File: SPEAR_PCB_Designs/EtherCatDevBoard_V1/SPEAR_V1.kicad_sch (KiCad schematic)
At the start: 32 parts, among them J2 USB_C_Receptacle_USB2.0_16P, J3 Conn_01x21_Pin, J5 Conn_01x21_Pin, J6 FTSH-107-01-F-DV-K-P-TR, SW1 SW_Push, SW2 SW_Push, U1 STM32F446RCTx, U2 USBLC6-2SC6, U3 AMS1117-3.3, Y1 16MHz

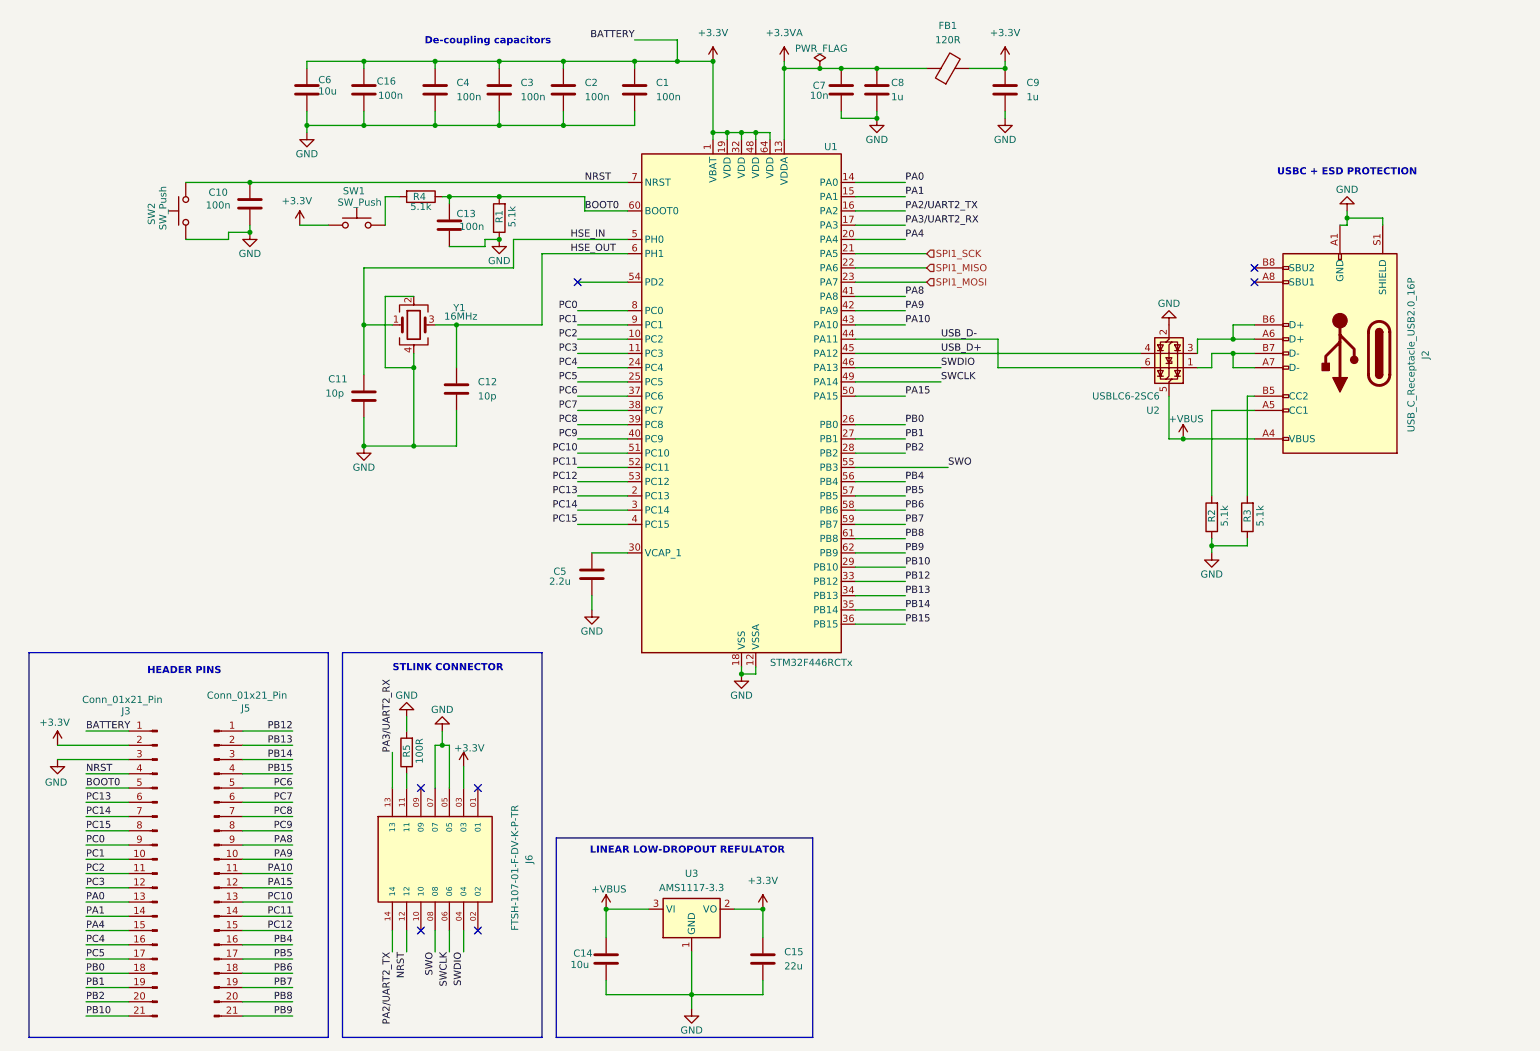
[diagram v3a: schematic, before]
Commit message: Update SPEAR_V1.kicad_sch
Footprints
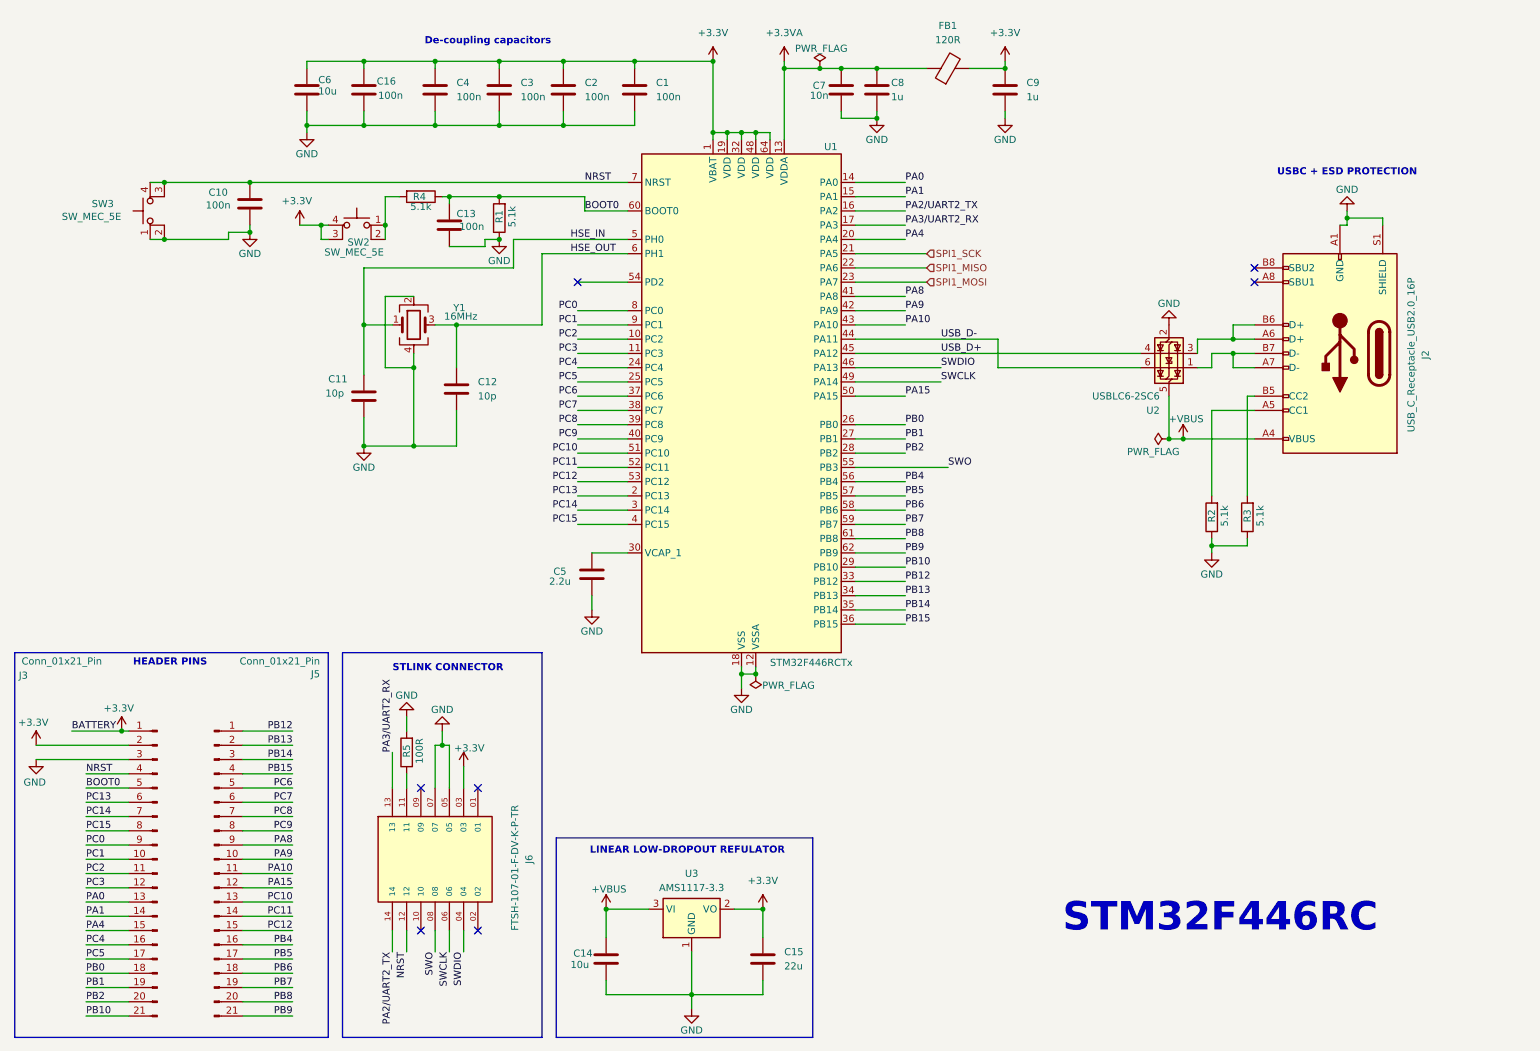
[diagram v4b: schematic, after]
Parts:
- removed SW1, SW2: SW_Push, symbol Switch:SW_Push
- added SW2, SW3: SW_MEC_5E, Button_Switch_SMD:SW_MEC_5GSH9, symbol Switch:SW_MEC_5E
- C1, C10, C11, C12, C13, C14, C16, C2, C3, C4, C5, C7, C8, C9: footprint (none) -> Capacitor_SMD:C_0402_1005Metric
- C15: footprint (none) -> Capacitor_SMD:C_0805_2012Metric
- C6: footprint (none) -> Capacitor_SMD:C_0603_1608Metric
- FB1: footprint (none) -> Inductor_SMD:L_0603_1608Metric
- J2: footprint (none) -> Connector_USB:USB_C_Receptacle_GCT_USB4105-xx-A_16P_TopMnt_Horizontal
- J3, J5: footprint (none) -> Connector_PinHeader_2.54mm:PinHeader_1x21_P2.54mm_Vertical
- J6: footprint FTSH-107-01-F-DV-K-P-TR:SAMTEC_FTSH-107-01-F-DV-K-P-TR -> Library:SAMTEC_FTSH-107-01-F-DV-K-P-TR
- R1, R2, R3, R4, R5: footprint (none) -> Resistor_SMD:R_0402_1005Metric
- Y1: footprint (none) -> Crystal:Crystal_SMD_2016-4Pin_2.0x1.6mm
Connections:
- net +3.3V: now also SW2.3 (K), SW2.4 (A)
- net GND: now also SW3.1, SW3.2
- net NRST: now also SW3.3 (K), SW3.4 (A)
- net at R4.2: now also SW2.1, SW2.2
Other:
- note added: "STM32F446RC"
- title: (none) -> SPEAR Development Board

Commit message: Updated Schematic and routing
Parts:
- removed C13: 100n, Capacitor_SMD:C_0402_1005Metric, symbol Device:C
- removed SW2, SW3: SW_MEC_5E, Button_Switch_SMD:SW_MEC_5GSH9, symbol Switch:SW_MEC_5E
- added D1: LED, LED_SMD:LED_0201_0603Metric, symbol Device:LED
- added R6: 5.1k, Resistor_SMD:R_0402_1005Metric, symbol Device:R
- added SW1: SW_Push, Button_Switch_SMD:SW_Tactile_SPST_NO_Straight_CK_PTS636Sx25SMTRLFS, symbol Switch:SW_Push
- R1: value 5.1k -> 10k
- R4: value 5.1k -> 100R
- Y1: footprint Crystal:Crystal_SMD_2016-4Pin_2.0x1.6mm -> Crystal:Crystal_SMD_3225-4Pin_3.2x2.5mm
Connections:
- net +3.3V: now also D1.2 (A)
- net BOOT0: now also R1.1; no longer J3.5 (Pin_5), R1.2, R4.1
- net GND: now also J3.4 (Pin_4), R1.2, R6.2, SW1.1; no longer R1.1
- net NRST: now also R4.1; no longer J3.4 (Pin_4)
- net PA0: now also J3.9 (Pin_9); no longer J3.13 (Pin_13)
- net PA1: now also J3.10 (Pin_10); no longer J3.14 (Pin_14)
- net PA10: now also J5.7 (Pin_7); no longer J5.11 (Pin_11)
- net PA15: now also J5.8 (Pin_8); no longer J5.12 (Pin_12)
- net PA4: now also J3.11 (Pin_11); no longer J3.15 (Pin_15)
- net PA8: now also J5.5 (Pin_5); no longer J5.9 (Pin_9)
- net PA9: now also J5.6 (Pin_6); no longer J5.10 (Pin_10)
- net PB0: now also J3.14 (Pin_14); no longer J3.18 (Pin_18)
- net PB1: now also J3.15 (Pin_15); no longer J3.19 (Pin_19)
- net PB10: now also J3.17 (Pin_17); no longer J3.21 (Pin_21)
- net PB12: now also J3.18 (Pin_18); no longer J5.1 (Pin_1)
- net PB13: now also J3.19 (Pin_19); no longer J5.2 (Pin_2)
- net PB14: now also J3.20 (Pin_20); no longer J5.3 (Pin_3)
- net PB15: now also J3.21 (Pin_21); no longer J5.4 (Pin_4)
- net PB2: now also J3.16 (Pin_16); no longer J3.20 (Pin_20)
- net PB4: now also J5.13 (Pin_13); no longer J5.16 (Pin_16)
- net PB5: now also J5.14 (Pin_14); no longer J5.17 (Pin_17)
- net PB6: now also J5.15 (Pin_15); no longer J5.18 (Pin_18)
- net PB7: now also J5.16 (Pin_16); no longer J5.19 (Pin_19)
- net PB8: now also J5.17 (Pin_17); no longer J5.20 (Pin_20)
- net PB9: now also J5.18 (Pin_18); no longer J5.21 (Pin_21)
- net PC0: now also J3.5 (Pin_5); no longer J3.9 (Pin_9)
- net PC1: now also J3.6 (Pin_6); no longer J3.10 (Pin_10)
- net PC10: now also J5.9 (Pin_9); no longer J5.13 (Pin_13)
- net PC11: now also J5.10 (Pin_10); no longer J5.14 (Pin_14)
- net PC12: now also J5.11 (Pin_11); no longer J5.15 (Pin_15)
- net PC13: now also J5.19 (Pin_19); no longer J3.6 (Pin_6)
- net PC14: now also J5.20 (Pin_20); no longer J3.7 (Pin_7)
- net PC15: now also J5.21 (Pin_21); no longer J3.8 (Pin_8)
- net PC2: now also J3.7 (Pin_7); no longer J3.11 (Pin_11)
- net PC3: now also J3.8 (Pin_8); no longer J3.12 (Pin_12)
- net PC4: now also J3.12 (Pin_12); no longer J3.16 (Pin_16)
- net PC5: now also J3.13 (Pin_13); no longer J3.17 (Pin_17)
- net PC6: now also J5.1 (Pin_1); no longer J5.5 (Pin_5)
- net PC7: now also J5.2 (Pin_2); no longer J5.6 (Pin_6)
- net PC8: now also J5.3 (Pin_3); no longer J5.7 (Pin_7)
- net PC9: now also J5.4 (Pin_4); no longer J5.8 (Pin_8)
- net at R4.2: now also SW1.2
- net PD2: now reaches U1.54 (PD2)
- net PD2: now also J5.12 (Pin_12)
- net USBC_D-: now reaches J2.A7 (D-), J2.B7 (D-), U2.1 (I/O1)
- net USBC_D+: now reaches J2.A6 (D+), J2.B6 (D+), U2.3 (I/O2)
- net +VBUS renamed +5V
- net PA2/UART2_TX renamed UART2_TX
- net PA3/UART2_RX renamed UART2_RX
- new net PWR_LED_K: D1.1 (K), R6.1
- no-connect marks 7 -> 6
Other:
- moved on the sheet: C10

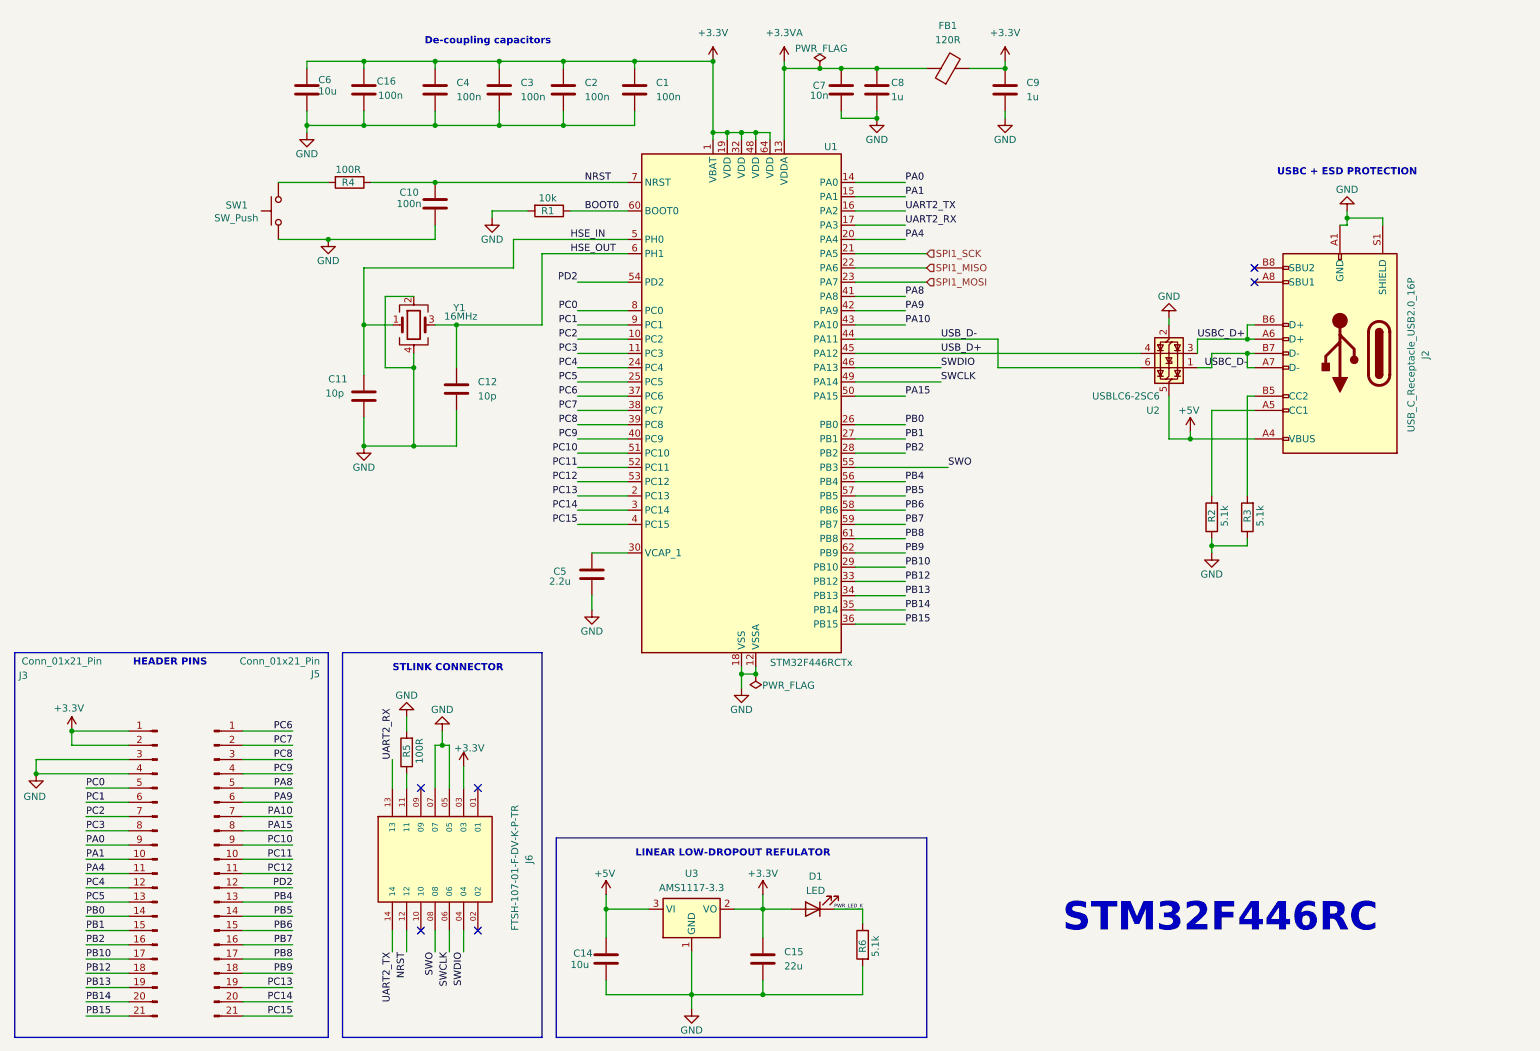
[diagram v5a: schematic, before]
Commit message: changes to lan setting
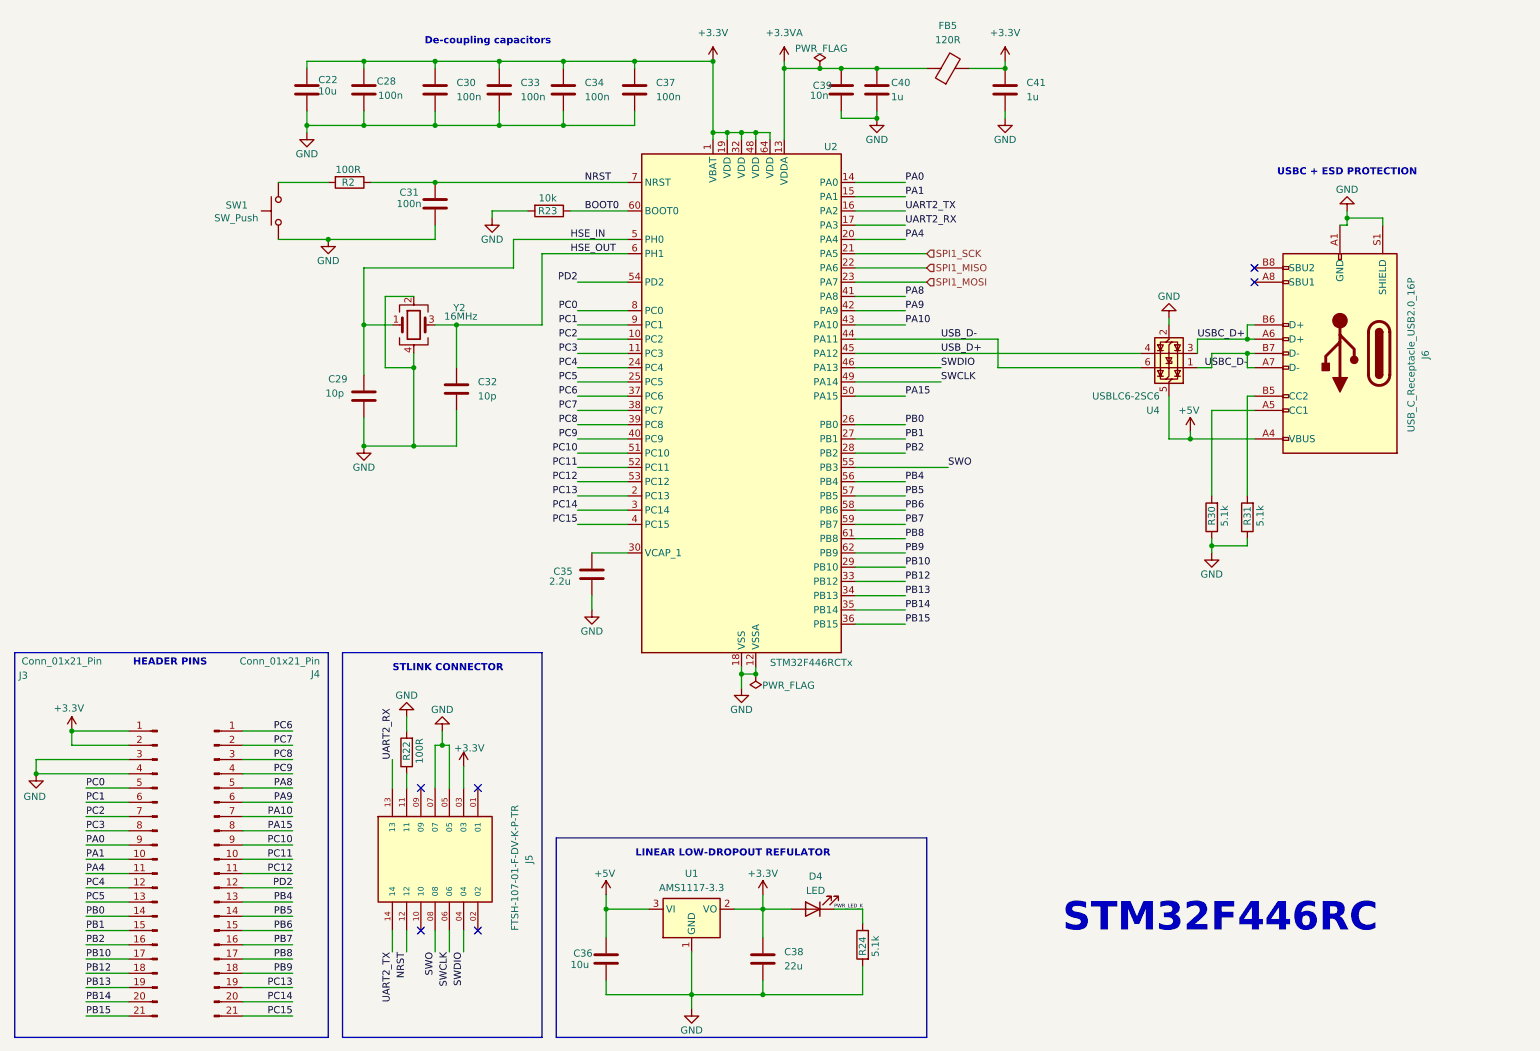
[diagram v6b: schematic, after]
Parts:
- renumbered C6 to C22, C16 to C28, C11 to C29, C4 to C30, C10 to C31, C12 to C32, C3 to C33, C2 to C34, C5 to C35, C14 to C36, C1 to C37, C15 to C38, C7 to C39, C8 to C40, C9 to C41, D1 to D4, FB1 to FB5, J5 to J4, J6 to J5, J2 to J6, R4 to R2, R5 to R22, R1 to R23, R6 to R24, R2 to R30, R3 to R31, U3 to U1, U1 to U2, U2 to U4, Y1 to Y2
